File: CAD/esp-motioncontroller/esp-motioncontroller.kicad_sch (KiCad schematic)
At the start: 4 parts

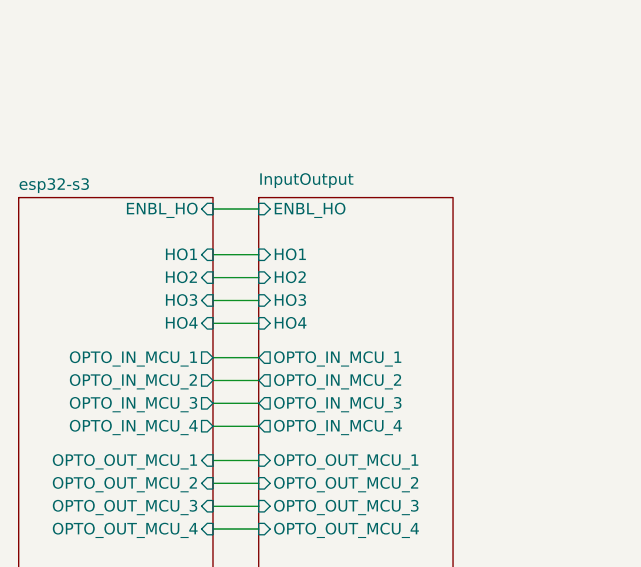
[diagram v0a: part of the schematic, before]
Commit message: Feat: Allmost complete sepdriver
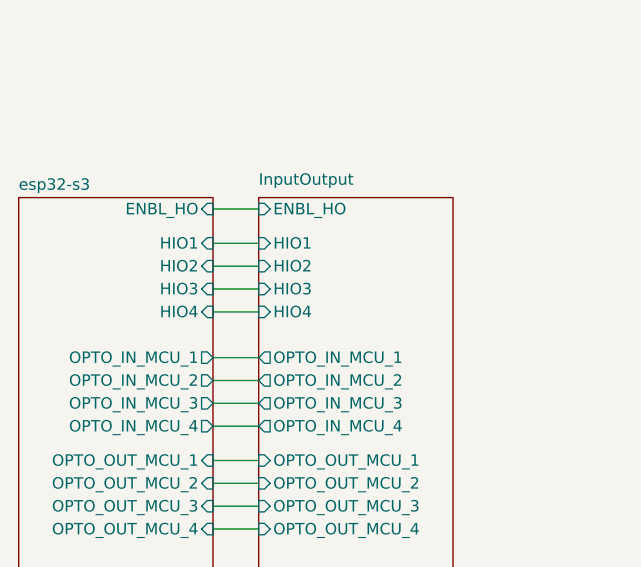
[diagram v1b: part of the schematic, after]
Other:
- sheet InputOutput ports: added HIO1, HIO2, HIO3, HIO4; removed HO1, HO2, HO3, HO4
- sheet esp32-s3 ports: added HIO1, HIO2, HIO3, HIO4; removed HO1, HO2, HO3, HO4
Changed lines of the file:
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@@
-	(wire
-		(pts
-			(xy 137.16 62.23) (xy 142.24 62.23)
-		)
-		(stroke
-			(width 0)
-			(type default)
-		)
-	)
 	(wire
 		(pts
@@
 	(wire
 		(pts
-			(xy 137.16 64.77) (xy 142.24 64.77)
+			(xy 137.16 60.96) (xy 142.24 60.96)
 		)
 		(stroke
@@
 	(wire
 		(pts
+			(xy 137.16 55.88) (xy 142.24 55.88)
+		)
+		(stroke
+			(width 0)
+			(type default)
+		)
+	)
+	(wire
+		(pts
 			(xy 137.16 87.63) (xy 142.24 87.63)
 		)
@@
 	(wire
 		(pts
-			(xy 137.16 57.15) (xy 142.24 57.15)
-		)
-		(stroke
-			(width 0)
-			(type default)
-		)
-	)
-	(wire
-		(pts
-			(xy 137.16 59.69) (xy 142.24 59.69)
-		)
-		(stroke
-			(width 0)
-			(type default)
-		)
-	)
-	(wire
-		(pts
 			(xy 137.16 76.2) (xy 142.24 76.2)
 		)
@@
 	(wire
 		(pts
+			(xy 137.16 63.5) (xy 142.24 63.5)
+		)
+		(stroke
+			(width 0)
+			(type default)
+		)
+	)
+	(wire
+		(pts
 			(xy 137.16 73.66) (xy 142.24 73.66)
+		)
+		(stroke
+			(width 0)
+			(type default)
+		)
+	)
+	(wire
+		(pts
+			(xy 137.16 58.42) (xy 142.24 58.42)
 		)
 		(stroke
@@
 			)
 		)
-		(pin "HO1" input
-			(at 142.24 57.15 180)
-			(effects
-				(font
-					(size 1.27 1.27)
-				)
-				(justify left)
-			)
-		)
-		(pin "HO2" input
-			(at 142.24 59.69 180)
-			(effects
-				(font
-					(size 1.27 1.27)
-				)
-				(justify left)
-			)
-		)
-		(pin "HO3" input
-			(at 142.24 62.23 180)
-			(effects
-				(font
-					(size 1.27 1.27)
-				)
-				(justify left)
-			)
-		)
-		(pin "HO4" input
-			(at 142.24 64.77 180)
-			(effects
-				(font
-					(size 1.27 1.27)
-				)
-				(justify left)
-			)
-		)
 		(pin "RE{slash}DE" input
 			(at 142.24 95.25 180)
@@
 		(pin "OPTO_OUT_MCU_4" input
 			(at 142.24 87.63 180)
+			(effects
+				(font
+					(size 1.27 1.27)
+				)
+				(justify left)
+			)
+		)
+		(pin "HIO1" input
+			(at 142.24 55.88 180)
+			(effects
+				(font
+					(size 1.27 1.27)
+				)
+				(justify left)
+			)
+		)
+		(pin "HIO2" input
+			(at 142.24 58.42 180)
+			(effects
+				(font
+					(size 1.27 1.27)
+				)
+				(justify left)
+			)
+		)
+		(pin "HIO3" input
+			(at 142.24 60.96 180)
+			(effects
+				(font
+					(size 1.27 1.27)
+				)
+				(justify left)
+			)
+		)
+		(pin "HIO4" input
+			(at 142.24 63.5 180)
 			(effects
 				(font
@@
 			)
 		)
-		(pin "HO1" input
-			(at 137.16 57.15 0)
-			(effects
-				(font
-					(size 1.27 1.27)
-				)
-				(justify right)
-			)
-		)
-		(pin "HO2" input
-			(at 137.16 59.69 0)
-			(effects
-				(font
-					(size 1.27 1.27)
-				)
-				(justify right)
-			)
-		)
-		(pin "HO3" input
-			(at 137.16 62.23 0)
-			(effects
-				(font
-					(size 1.27 1.27)
-				)
-				(justify right)
-			)
-		)
-		(pin "HO4" input
-			(at 137.16 64.77 0)
-			(effects
-				(font
-					(size 1.27 1.27)
-				)
-				(justify right)
-			)
-		)
 		(pin "RE{slash}DE" input
 			(at 137.16 95.25 0)
@@
 			(effects
 				(font
+					(size 1.27 1.27)
+				)
+				(justify right)
+			)
+		)
+		(pin "HIO1" input
+			(at 137.16 55.88 0)
+			(effects
+				(font
+					(size 1.27 1.27)
+				)
+				(justify right)
+			)
+		)
+		(pin "HIO2" input
+			(at 137.16 58.42 0)
+			(effects
+				(font
+					(size 1.27 1.27)
+				)
+				(justify right)
+			)
+		)
+		(pin "HIO3" input
+			(at 137.16 60.96 0)
+			(effects
+				(font
+					(size 1.27 1.27)
+				)
+				(justify right)
+			)
+		)
+		(pin "HIO4" input
+			(at 137.16 63.5 0)
+			(effects
+				(font
